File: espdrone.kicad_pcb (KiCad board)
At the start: 6 copper layers, 167.9 x 121.5 mm, 512 parts, among them J10 Conn_01x04, J11 Conn_01x04, J12 Conn_01x04, J4 Conn_01x06, J5 Conn_Coaxial, J6 Conn_01x06, J7 Conn_01x06, J8 Conn_01x04, J9 Conn_01x04, Q1 NMOS, Q10 NMOS, Q11 NMOS, Q12 NMOS, Q13 NMOS, Q14 NMOS, Q15 NMOS, Q16 NMOS, Q17 NMOS, Q18 NMOS, Q19 NMOS, Q2 NMOS, Q20 NMOS, Q21 NMOS, Q22 NMOS, Q23 NMOS, Q24 NMOS, Q25 NMOS, Q26 NMOS, Q27 NMOS, Q28 NMOS, Q3 NMOS, Q4 NMOS, Q5 NMOS, Q6 NMOS, Q7 NMOS, Q8 NMOS, Q9 NMOS, U10 FPC-1.0FX-15PWCR-H20, U11 VL53L1CXV0FY1, U12 LIS2MDL, U13 LSM6DS3, U14 PMW3901MB-TXQT_C43496881, U15 STM32G071K8U6, U16 DRV8328ARUYR, U18 STM32G071K8U6, U19 DRV8328ARUYR, U2 USBLC6-2P6, U20 INA180A2, U21 STM32G071K8U6, U22 DRV8328ARUYR, U23 INA180A2, U24 STM32G071K8U6, U25 DRV8328ARUYR, U26 INA180A2, U27 INA190A3IDCKR, U28 INA190A3IDCKR, U29 INA190A3IDCKR, U3 W25Q128JVP, U4 ESP32-C5HF4, U5 LFD182G45DCHD277, U6 TLV62569DBV, U7 INA190A3IDCKR, U8 TPS63070RNMR, U9 TPS2121RUXR, Y1 Crystal_GND24, Y2 Crystal_GND24

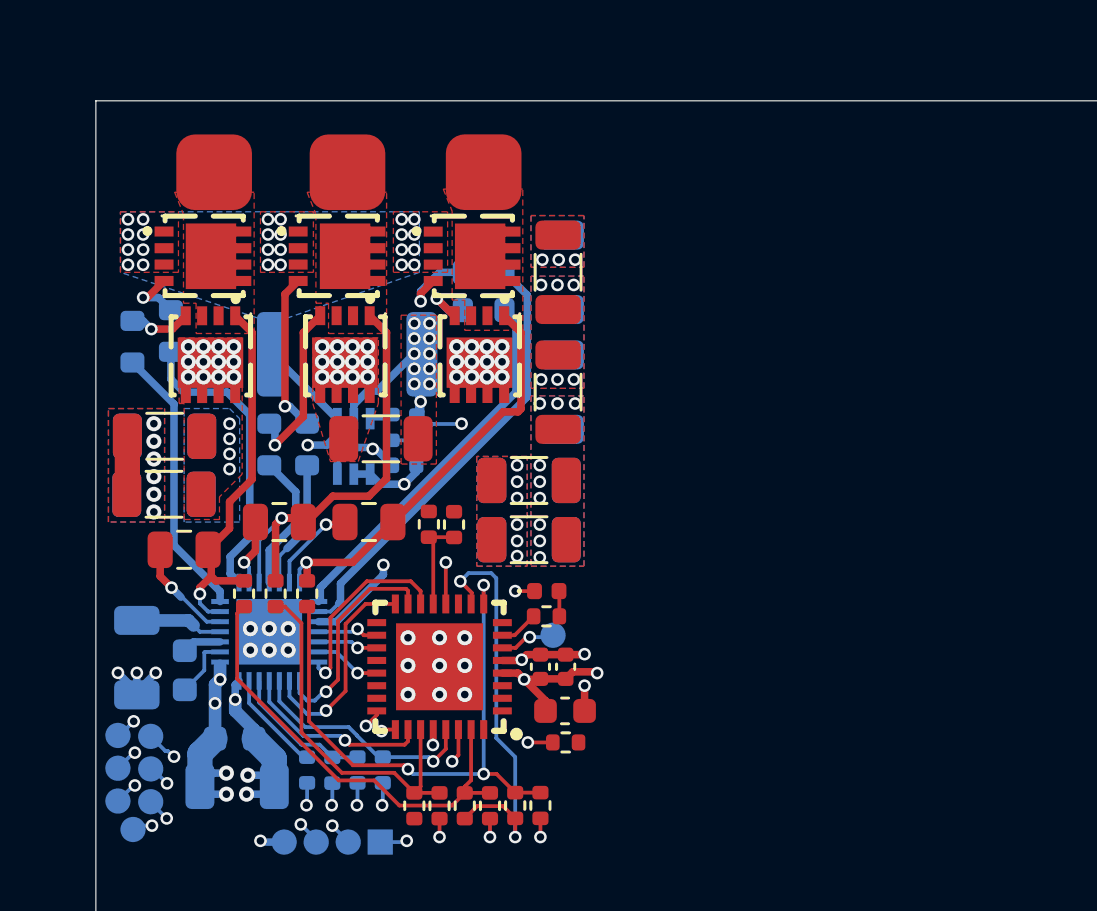
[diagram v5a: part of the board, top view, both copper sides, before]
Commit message: Add moar caps
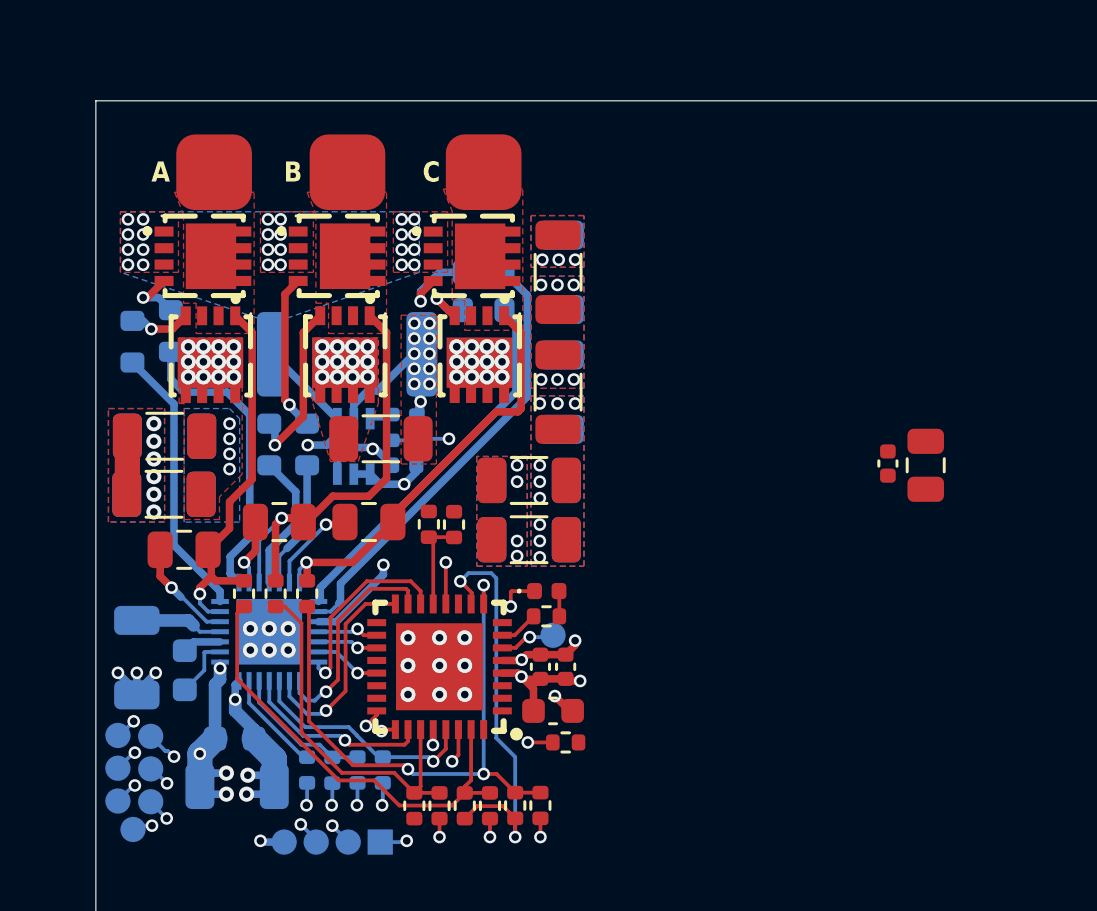
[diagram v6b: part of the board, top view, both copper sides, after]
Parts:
- added C112: 100n, Capacitor_SMD:C_0402_1005Metric, F.Cu at (161.7, 109.1)
- added C115: 1u, Capacitor_SMD:C_0805_2012Metric, F.Cu at (163.2, 109.2)
- moved C108 0.47 mm to (148.4, 118.9)
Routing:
- net /Motors/ESC1/ISENSE: track 10.6 -> 8.91 mm
- net +3V3: track 12.1 -> 11.3 mm
- net GND: track 33.7 -> 34.3 mm, vias 61 -> 59
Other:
- board text added: "A"
- board text added: "B"
- board text added: "C"
- board text added: "H"
- board text added: "L"
- board text added: "clk"
- board text added: "dio"
- board text added: "nrst"
